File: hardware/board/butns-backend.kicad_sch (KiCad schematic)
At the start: 3 parts, among them U1 Pico, U2 74LVC1G17

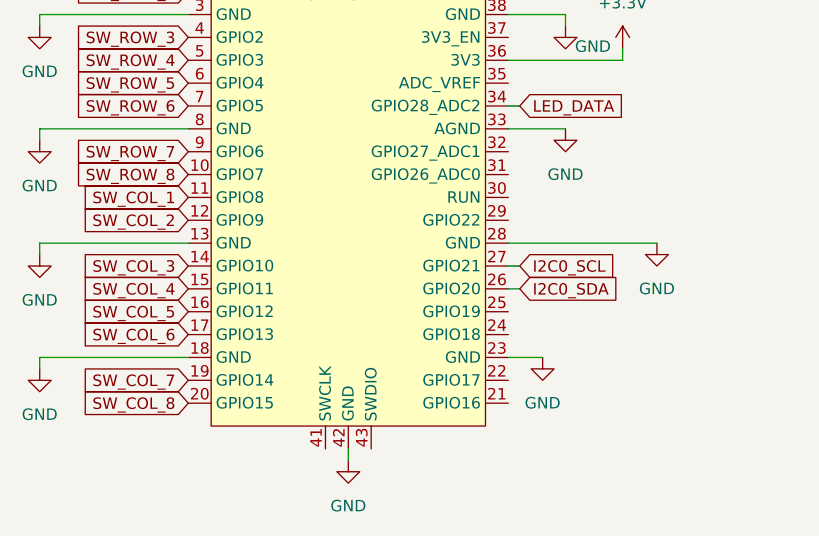
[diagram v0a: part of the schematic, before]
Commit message: Convert to 16x8 grid (8 rows x 16 columns)
Hardware
- PCB extended to 190.44 x 99 mm with eight additional columns:
  128 switches, 128 diodes, 128 SK6812-EC20, 129 capacitors
- New column nets SW_COL_8..15 on GPIO16-22 and GPIO26, former
  SW_COL_8 (GPIO15) is now SW_COL_16
- LED chain runs row by row over 16 columns
- Tilt header J1 and I2C nets removed, GPIO27 left free
- Second inner mounting hole H6
- Schematic: new sheet butns-frontend2 with the 64 added cells,
  frontend and backend sheets adapted
- Regenerated jlcpcb/ gerbers, BOM and CPL, new butns.step,
  removed stale 8x8 butns.stl and model/butns.wrl

Firmware
- 16 column matrix scan per column with settle time
- LED index row * 16 + col, rotation limited to 0 and 180 degrees
- LED current estimate limited to MAX_LED_CURRENT_MA
- MPU6050 tilt support removed
- Fix led/level/row and led/level/col offset handling

Case
- case.scad and buttons.scad extended to 16 columns, second standoff
- Explicit apply_to argument for roundedcube calls

Co-Authored-By: Claude Opus 5.5 <noreply@anthropic.com>
Claude-Session: https://claude.ai/code/session_0195H63MEXeeVZ7CNyHAeb6N
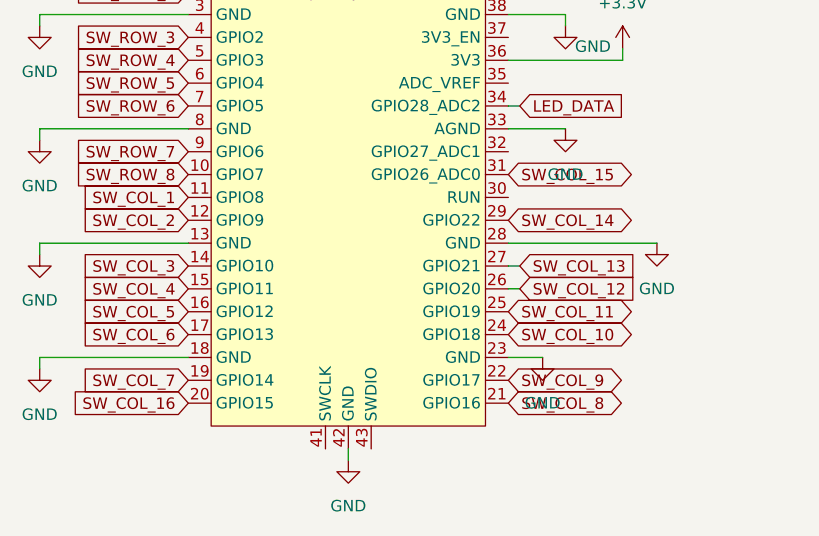
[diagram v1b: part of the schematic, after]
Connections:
- net SW_COL_8: now also U1.21 (GPIO16); no longer U1.20 (GPIO15)
- net SW_COL_9: now reaches U1.22 (GPIO17)
- net SW_COL_10: now reaches U1.24 (GPIO18)
- net SW_COL_11: now reaches U1.25 (GPIO19)
- net SW_COL_14: now reaches U1.29 (GPIO22)
- net SW_COL_15: now reaches U1.31 (GPIO26_ADC0)
- net I2C0_SCL renamed SW_COL_13
- net I2C0_SDA renamed SW_COL_12
- new net SW_COL_16: U1.20 (GPIO15)
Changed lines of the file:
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@@
 		)
 	)
-	(global_label "SW_COL_8"
+	(global_label "SW_COL_16"
 		(shape input)
 		(at 110.49 109.22 180)
@@
 		)
 	)
-	(global_label "I2C0_SCL"
+	(global_label "SW_COL_13"
 		(shape input)
 		(at 147.32 93.98 0)
@@
 		)
 	)
-	(global_label "I2C0_SDA"
+	(global_label "SW_COL_12"
 		(shape input)
 		(at 147.32 96.52 0)
@@
 			)
 		)
+	)
+	(global_label "SW_COL_8"
+		(shape bidirectional)
+		(at 146.05 109.22 0)
+		(fields_autoplaced yes)
+		(effects
+			(font
+				(size 1.27 1.27)
+			)
+			(justify left)
+		)
+		(property "Intersheetrefs" "${INTERSHEET_REFS}"
+			(at 146.05 109.22 0)
+			(effects
+				(font
+					(size 1.27 1.27)
+				)
+				(hide yes)
+			)
+		)
+	)
+	(global_label "SW_COL_9"
+		(shape bidirectional)
+		(at 146.05 106.68 0)
+		(fields_autoplaced yes)
+		(effects
+			(font
+				(size 1.27 1.27)
+			)
+			(justify left)
+		)
+		(property "Intersheetrefs" "${INTERSHEET_REFS}"
+			(at 146.05 106.68 0)
+			(effects
+				(font
+					(size 1.27 1.27)
+				)
+				(hide yes)
+			)
+		)
+	)
+	(global_label "SW_COL_10"
+		(shape bidirectional)
+		(at 146.05 101.6 0)
+		(fields_autoplaced yes)
+		(effects
+			(font
+				(size 1.27 1.27)
+			)
+			(justify left)
+		)
+		(property "Intersheetrefs" "${INTERSHEET_REFS}"
+			(at 146.05 101.6 0)
+			(effects
+				(font
+					(size 1.27 1.27)
+				)
+				(hide yes)
+			)
+		)
+	)
+	(global_label "SW_COL_11"
+		(shape bidirectional)
+		(at 146.05 99.06 0)
+		(fields_autoplaced yes)
+		(effects
+			(font
+				(size 1.27 1.27)
+			)
+			(justify left)
+		)
+		(property "Intersheetrefs" "${INTERSHEET_REFS}"
+			(at 146.05 99.06 0)
+			(effects
+				(font
+					(size 1.27 1.27)
+				)
+				(hide yes)
+			)
+		)
+	)
+	(global_label "SW_COL_14"
+		(shape bidirectional)
+		(at 146.05 88.9 0)
+		(fields_autoplaced yes)
+		(effects
+			(font
+				(size 1.27 1.27)
+			)
+			(justify left)
+		)
+		(property "Intersheetrefs" "${INTERSHEET_REFS}"
+			(at 146.05 88.9 0)
+			(effects
+				(font
+					(size 1.27 1.27)
+				)
+				(hide yes)
+			)
+		)
+	)
+	(global_label "SW_COL_15"
+		(shape bidirectional)
+		(at 146.05 83.82 0)
+		(fields_autoplaced yes)
+		(effects
+			(font
+				(size 1.27 1.27)
+			)
+			(justify left)
+		)
+		(property "Intersheetrefs" "${INTERSHEET_REFS}"
+			(at 146.05 83.82 0)
+			(effects
+				(font
+					(size 1.27 1.27)
+				)
+				(hide yes)
+			)
+		)
